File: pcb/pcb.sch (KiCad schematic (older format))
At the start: 1 part, among them U1 NodeMCU1.0(ESP-12E)

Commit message: First PCB revision complete
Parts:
- added R1: 10K, Resistor_THT:R_Axial_DIN0204_L3.6mm_D1.6mm_P7.62mm_Horizontal, symbol Device:R
- added U2: DHT22, Connector_PinSocket_2.54mm:PinSocket_1x04_P2.54mm_Horizontal, symbol sensors:DHT22
- added U3: SSD1306_OLED_128x32, personal:SSD1306_OLED_128x32, symbol sensors:SSD1306_OLED_128x32
- added U4: VL6180X_Adafruit, personal:VL6180X_Adafruit, symbol sensors:VL6180X_Adafruit
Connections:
- net GND: now reaches U1.10 (GND)
- net GND: now also U1.17 (GND), U1.24 (GND), U2.1 (GND), U3.4 (GND), U4.5 (GND)
- net +3V3: now reaches U1.11 (3.3V)
- net +3V3: now also U1.16 (3.3V), U1.25 (3.3V), R1.1, U2.4 (VCC), U3.3 (VCC), U4.7 (Vin)
- net SDA: now reaches U1.28 (D2(GPIO4))
- net SDA: now also U3.1 (SDA), U4.1 (SDA)
- net SCL: now reaches U1.29 (D1(GPIO5))
- net SCL: now also U3.2 (SCL), U4.2 (SCL)
- net at U1.4 (SD3(GPIO10)): now also R1.2, U2.3 (Data)
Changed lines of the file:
@@
 EESchema Schematic File Version 4
+LIBS:pcb-cache
 EELAYER 26 0
 EELAYER END
@@
 	1    0    0    -1
 $EndComp
+$Comp
+L sensors:DHT22 U2
+U 1 1 5EB9C5AE
+P 3850 3650
+F 0 "U2" H 4027 3746 50  0000 L CNN
+F 1 "DHT22" H 4027 3655 50  0000 L CNN
+F 2 "Connector_PinSocket_2.54mm:PinSocket_1x04_P2.54mm_Horizontal" H 3700 3750 50  0001 C CNN
+F 3 "" H 3700 3750 50  0001 C CNN
+	1    3850 3650
+	-1   0    0    -1
+$EndComp
+$Comp
+L sensors:SSD1306_OLED_128x32 U3
+U 1 1 5EBADA8A
+P 9050 3400
+F 0 "U3" H 9050 3800 50  0000 L CNN
+F 1 "SSD1306_OLED_128x32" H 8700 3700 50  0000 L CNN
+F 2 "personal:SSD1306_OLED_128x32" H 8550 3750 50  0001 C CNN
+F 3 "" H 8550 3750 50  0001 C CNN
+	1    9050 3400
+	1    0    0    -1
+$EndComp
+$Comp
+L Device:R R1
+U 1 1 5EBADE24
+P 4500 3400
+F 0 "R1" H 4430 3446 50  0000 R CNN
+F 1 "10K" H 4430 3355 50  0000 R CNN
+F 2 "Resistor_THT:R_Axial_DIN0204_L3.6mm_D1.6mm_P7.62mm_Horizontal" V 4430 3400 50  0001 C CNN
+F 3 "~" H 4500 3400 50  0001 C CNN
+	1    4500 3400
+	-1   0    0    -1
+$EndComp
+$Comp
+L power:GND #PWR0101
+U 1 1 5EBADF75
+P 4100 3750
+F 0 "#PWR0101" H 4100 3500 50  0001 C CNN
+F 1 "GND" H 4105 3577 50  0000 C CNN
+F 2 "" H 4100 3750 50  0001 C CNN
+F 3 "" H 4100 3750 50  0001 C CNN
+	1    4100 3750
+	-1   0    0    -1
+$EndComp
+$Comp
+L power:+3.3V #PWR0102
+U 1 1 5EBADFC6
+P 4250 3200
+F 0 "#PWR0102" H 4250 3050 50  0001 C CNN
+F 1 "+3.3V" H 4265 3373 50  0000 C CNN
+F 2 "" H 4250 3200 50  0001 C CNN
+F 3 "" H 4250 3200 50  0001 C CNN
+	1    4250 3200
+	-1   0    0    -1
+$EndComp
+Wire Wire Line
+	4100 3450 4250 3450
+Wire Wire Line
+	4250 3450 4250 3250
+Wire Wire Line
+	4500 3250 4250 3250
+Connection ~ 4250 3250
+Wire Wire Line
+	4250 3250 4250 3200
+Wire Wire Line
+	4100 3550 4500 3550
+Wire Wire Line
+	5250 3550 4500 3550
+Connection ~ 4500 3550
+$Comp
+L power:+3.3V #PWR0103
+U 1 1 5EBAE54C
+P 7100 4650
+F 0 "#PWR0103" H 7100 4500 50  0001 C CNN
+F 1 "+3.3V" H 7115 4823 50  0000 C CNN
+F 2 "" H 7100 4650 50  0001 C CNN
+F 3 "" H 7100 4650 50  0001 C CNN
+	1    7100 4650
+	1    0    0    -1
+$EndComp
+Text GLabel 7100 3450 3    50   Input ~ 0
+SDA
+Text GLabel 7100 3350 1    50   Input ~ 0
+SCL
+$Comp
+L sensors:VL6180X_Adafruit U4
+U 1 1 5EBAEF0A
+P 8950 4600
+F 0 "U4" H 8975 5065 50  0000 C CNN
+F 1 "VL6180X_Adafruit" H 8975 4974 50  0000 C CNN
+F 2 "personal:VL6180X_Adafruit" H 9000 4250 50  0001 C CNN
+F 3 "" H 9000 4250 50  0001 C CNN
+	1    8950 4600
+	1    0    0    -1
+$EndComp
+$Comp
+L power:+3.3V #PWR0104
+U 1 1 5EBAF0BC
+P 9400 4450
+F 0 "#PWR0104" H 9400 4300 50  0001 C CNN
+F 1 "+3.3V" H 9415 4623 50  0000 C CNN
+F 2 "" H 9400 4450 50  0001 C CNN
+F 3 "" H 9400 4450 50  0001 C CNN
+	1    9400 4450
+	1    0    0    -1
+$EndComp
+$Comp
+L power:GND #PWR0105
+U 1 1 5EBAF0F4
+P 9400 4650
+F 0 "#PWR0105" H 9400 4400 50  0001 C CNN
+F 1 "GND" H 9405 4477 50  0000 C CNN
+F 2 "" H 9400 4650 50  0001 C CNN
+F 3 "" H 9400 4650 50  0001 C CNN
+	1    9400 4650
+	1    0    0    -1
+$EndComp
+$Comp
+L power:GND #PWR0106
+U 1 1 5EBAF125
+P 8450 3500
+F 0 "#PWR0106" H 8450 3250 50  0001 C CNN
+F 1 "GND" H 8455 3327 50  0000 C CNN
+F 2 "" H 8450 3500 50  0001 C CNN
+F 3 "" H 8450 3500 50  0001 C CNN
+	1    8450 3500
+	1    0    0    -1
+$EndComp
+Wire Wire Line
+	8450 3200 8100 3200
+Wire Wire Line
+	8100 3200 8100 3450
+Wire Wire Line
+	8100 4400 8550 4400
+Wire Wire Line
+	8450 3300 8150 3300
+Wire Wire Line
+	8150 3300 8150 3350
+Wire Wire Line
+	8150 4500 8550 4500
+Text GLabel 7200 4650 2    50   Input ~ 0
+3v3
+Text GLabel 8450 3400 0    50   Input ~ 0
+3v3
+Wire Wire Line
+	6850 3450 8100 3450
+Connection ~ 8100 3450
+Wire Wire Line
+	8100 3450 8100 4400
+Wire Wire Line
+	6850 3350 8150 3350
+Connection ~ 8150 3350
+Wire Wire Line
+	8150 3350 8150 4500
+Wire Wire Line
+	6850 4650 7100 4650
+Wire Wire Line
+	7100 4650 7200 4650
+Connection ~ 7100 4650
+$Comp
+L power:GND #PWR0107
+U 1 1 5EBAFEB9
+P 6950 4850
+F 0 "#PWR0107" H 6950 4600 50  0001 C CNN
+F 1 "GND" H 6955 4677 50  0000 C CNN
+F 2 "" H 6950 4850 50  0001 C CNN
+F 3 "" H 6950 4850 50  0001 C CNN
+	1    6950 4850
+	1    0    0    -1
+$EndComp
+Wire Wire Line
+	6850 4550 6950 4550
+Text GLabel 6850 3750 2    50   Input ~ 0
+3v3
+Text GLabel 6850 3850 2    50   Input ~ 0
+GND
+Text GLabel 6950 4750 2    50   Input ~ 0
+GND
+Wire Wire Line
+	6950 4550 6950 4850
+Text GLabel 5250 4150 0    50   Input ~ 0
+GND
+Text GLabel 5250 4250 0    50   Input ~ 0
+3v3
 $EndSCHEMATC

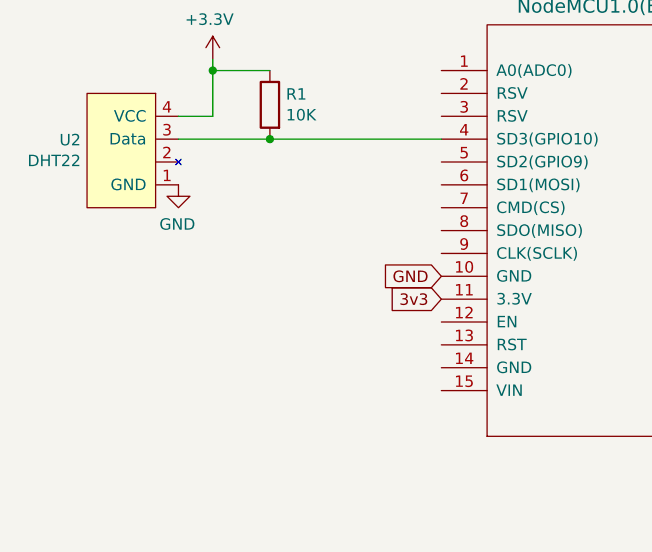
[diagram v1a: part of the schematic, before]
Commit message: Add push button
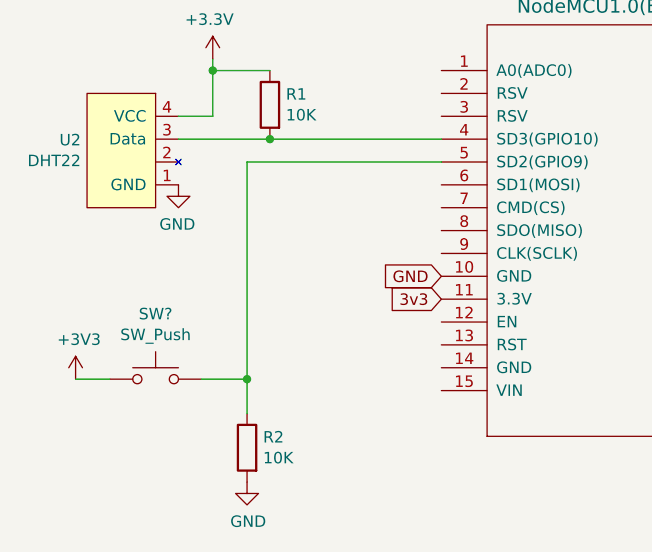
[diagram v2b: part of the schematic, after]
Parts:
- added R2: 10K, Resistor_THT:R_Axial_DIN0204_L3.6mm_D1.6mm_P7.62mm_Horizontal, symbol Device:R
- added SW?: SW_Push, Button_Switch_THT:SW_PUSH_6mm, symbol Switch:SW_Push
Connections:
- net +3V3: now also SW?.1
- net GND: now also R2.2
- net at U1.5 (SD2(GPIO9)): now also R2.1, SW?.2
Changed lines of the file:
@@
 Text GLabel 5250 4250 0    50   Input ~ 0
 3v3
+$Comp
+L Switch:SW_Push SW?
+U 1 1 5EBB1E95
+P 4000 4600
+F 0 "SW?" H 4000 4885 50  0000 C CNN
+F 1 "SW_Push" H 4000 4794 50  0000 C CNN
+F 2 "Button_Switch_THT:SW_PUSH_6mm" H 4000 4800 50  0001 C CNN
+F 3 "" H 4000 4800 50  0001 C CNN
+	1    4000 4600
+	1    0    0    -1
+$EndComp
+Wire Wire Line
+	4200 4600 4400 4600
+Wire Wire Line
+	4400 4600 4400 3650
+Wire Wire Line
+	4400 3650 5250 3650
+$Comp
+L power:GND #PWR?
+U 1 1 5EBB2A8D
+P 4400 5050
+F 0 "#PWR?" H 4400 4800 50  0001 C CNN
+F 1 "GND" H 4405 4877 50  0000 C CNN
+F 2 "" H 4400 5050 50  0001 C CNN
+F 3 "" H 4400 5050 50  0001 C CNN
+	1    4400 5050
+	1    0    0    -1
+$EndComp
+$Comp
+L Device:R R2
+U 1 1 5EBB2B1E
+P 4400 4900
+F 0 "R2" H 4330 4946 50  0000 R CNN
+F 1 "10K" H 4330 4855 50  0000 R CNN
+F 2 "Resistor_THT:R_Axial_DIN0204_L3.6mm_D1.6mm_P7.62mm_Horizontal" V 4330 4900 50  0001 C CNN
+F 3 "~" H 4400 4900 50  0001 C CNN
+	1    4400 4900
+	-1   0    0    -1
+$EndComp
+Wire Wire Line
+	4400 4750 4400 4600
+Connection ~ 4400 4600
+$Comp
+L power:+3V3 #PWR?
+U 1 1 5EBB32E0
+P 3650 4600
+F 0 "#PWR?" H 3650 4450 50  0001 C CNN
+F 1 "+3V3" H 3665 4773 50  0000 C CNN
+F 2 "" H 3650 4600 50  0001 C CNN
+F 3 "" H 3650 4600 50  0001 C CNN
+	1    3650 4600
+	1    0    0    -1
+$EndComp
+Wire Wire Line
+	3650 4600 3800 4600
 $EndSCHEMATC

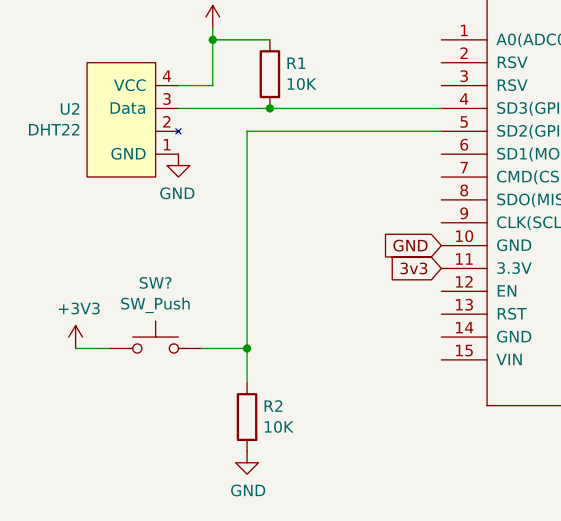
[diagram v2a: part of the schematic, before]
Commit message: Correct display footprint to right size
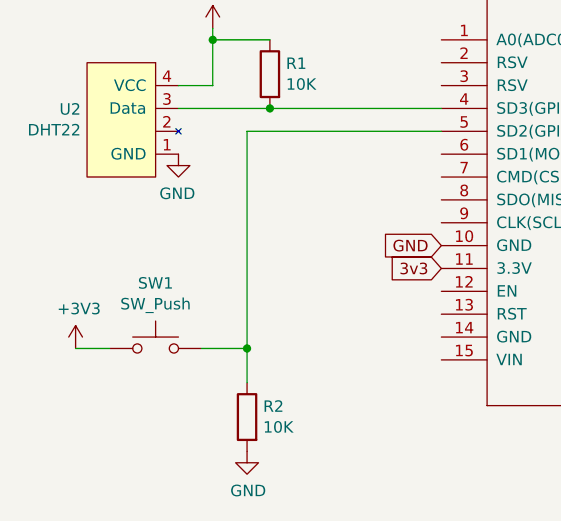
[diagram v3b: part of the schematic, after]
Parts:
- U3: footprint personal:SSD1306_OLED_128x32 -> personal:SSD1306_Adafruit_128x32
- gave numbers to parts that had none: 1
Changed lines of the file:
@@
 F 0 "U3" H 9050 3800 50  0000 L CNN
 F 1 "SSD1306_OLED_128x32" H 8700 3700 50  0000 L CNN
-F 2 "personal:SSD1306_OLED_128x32" H 8550 3750 50  0001 C CNN
+F 2 "personal:SSD1306_Adafruit_128x32" H 8550 3750 50  0001 C CNN
 F 3 "" H 8550 3750 50  0001 C CNN
 	1    9050 3400
@@
 3v3
 $Comp
-L Switch:SW_Push SW?
+L Switch:SW_Push SW1
 U 1 1 5EBB1E95
 P 4000 4600
-F 0 "SW?" H 4000 4885 50  0000 C CNN
+F 0 "SW1" H 4000 4885 50  0000 C CNN
 F 1 "SW_Push" H 4000 4794 50  0000 C CNN
 F 2 "Button_Switch_THT:SW_PUSH_6mm" H 4000 4800 50  0001 C CNN
@@
 	4400 3650 5250 3650
 $Comp
-L power:GND #PWR?
+L power:GND #PWR0108
 U 1 1 5EBB2A8D
 P 4400 5050
-F 0 "#PWR?" H 4400 4800 50  0001 C CNN
+F 0 "#PWR0108" H 4400 4800 50  0001 C CNN
 F 1 "GND" H 4405 4877 50  0000 C CNN
 F 2 "" H 4400 5050 50  0001 C CNN
@@
 Connection ~ 4400 4600
 $Comp
-L power:+3V3 #PWR?
+L power:+3V3 #PWR0109
 U 1 1 5EBB32E0
 P 3650 4600
-F 0 "#PWR?" H 3650 4450 50  0001 C CNN
+F 0 "#PWR0109" H 3650 4450 50  0001 C CNN
 F 1 "+3V3" H 3665 4773 50  0000 C CNN
 F 2 "" H 3650 4600 50  0001 C CNN

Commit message: Use the right ESP8266 footprint
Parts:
- U1: footprint ESP8266:NodeMCU1.0(12-E) -> ESP8266:ESP12F-Devkit-V3
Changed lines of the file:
@@
 F 0 "U1" H 6050 5037 60  0000 C CNN
 F 1 "NodeMCU1.0(ESP-12E)" H 6050 4931 60  0000 C CNN
-F 2 "ESP8266:NodeMCU1.0(12-E)" H 5450 3100 60  0001 C CNN
+F 2 "ESP8266:ESP12F-Devkit-V3" H 5450 3100 60  0001 C CNN
 F 3 "" H 5450 3100 60  0000 C CNN
 	1    6050 3950
